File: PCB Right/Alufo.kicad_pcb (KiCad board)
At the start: 2 copper layers, 282.6 x 90.9 mm, 95 parts, among them J2 USB_C_Receptacle_USB2.0_16P_2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, J4 USB_C_Receptacle_USB2.0_16P_2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, K11 PG1350, K12 PG1350, K13 PG1350, K14 PG1350, K15 PG1350, K16 PG1350, K21 PG1350, K22 PG1350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

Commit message: Add additional pads to USB ports for strength
Also apply tweaks from left PCB to right.
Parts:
- D2: footprint Diode_SMD:D_SOD-323 -> BGK_Kicad:D_SOD-323
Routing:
- net Net-(FB2-Pad1): track 3.01 -> 2.23 mm
- net VCC: track 52.0 -> 51.2 mm
- net USB_P-: track 5.48 -> 6.10 mm
- net Row1: track 116.3 -> 115.8 mm
- net +3V3: track 85.7 -> 85.2 mm

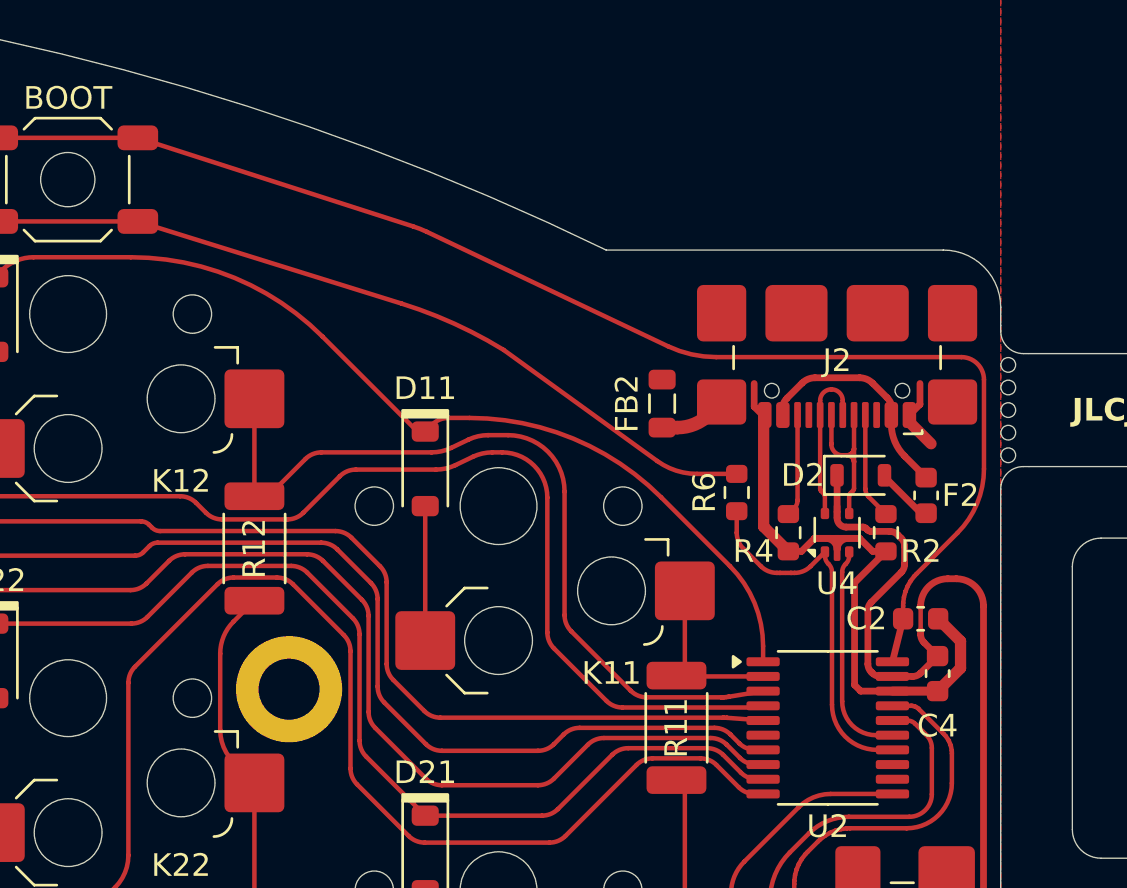
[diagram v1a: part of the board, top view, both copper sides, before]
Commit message: Move righthand USB port in
Moved port and associated components 19.05÷12mm left to account for SMD legs.
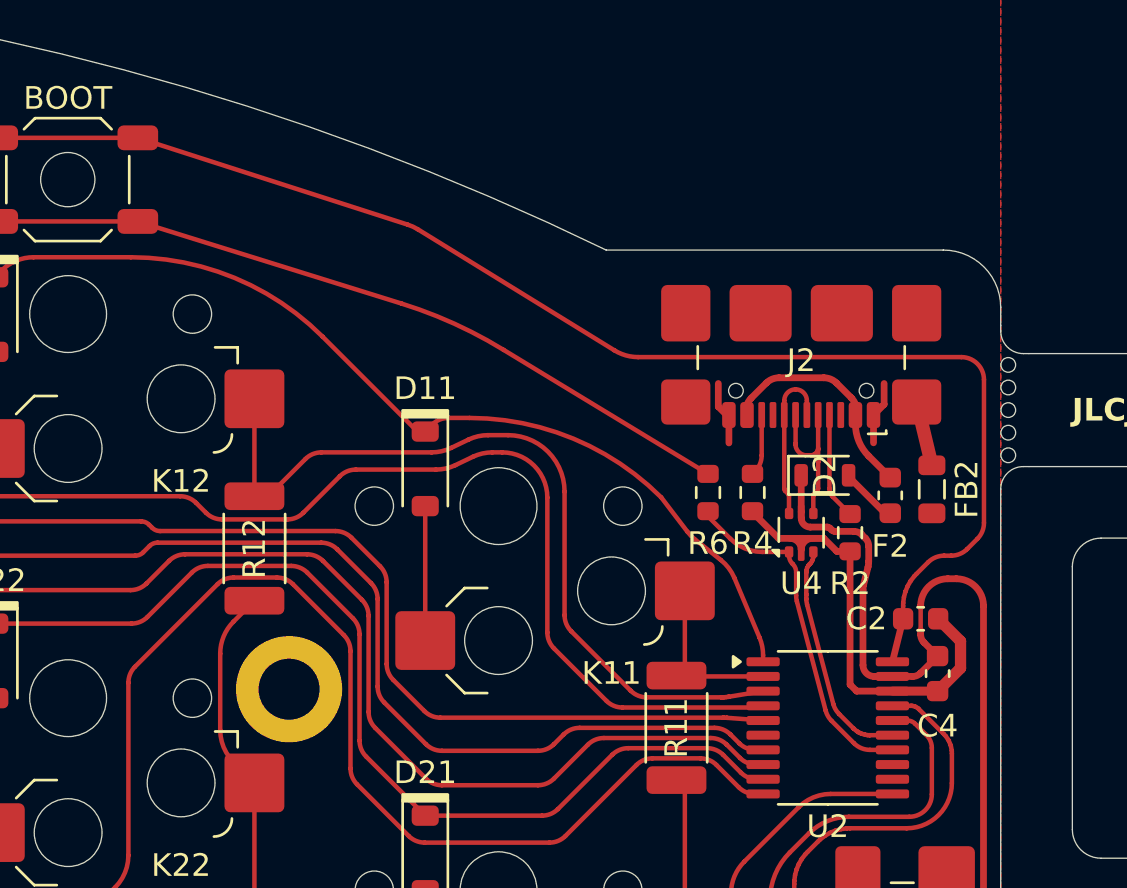
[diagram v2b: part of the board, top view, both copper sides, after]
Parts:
- removed NT2: NetTie_2, Project_Library:NetTie-2_SMD_Pad0.2mm
- moved FB2 12.5 mm to (162.1, 51.7), turned to -90 degrees
- moved R4 2.38 mm to (154.1, 51.8)
- moved D2 1.59 mm to (157.3, 51.1)
- moved F2 1.59 mm to (160.2, 51.9)
- moved J2 1.59 mm to (156.3, 44.7)
- moved R2 1.59 mm to (158.4, 53.6)
- moved U4 1.59 mm to (156.3, 53.6)
- moved R6 1.27 mm to (152.1, 51.8)
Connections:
- J2 pad S1: Net-(FB2-Pad1) -> unconnected-(J2-SHIELD-PadS1)
- J2 pad S2: unconnected-(J2-SHIELD-PadS2) -> Net-(FB2-Pad1)
- R6 pad 1: Net-(NT2-Pad2) -> USB+
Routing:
- net GND: track 33.9 -> 28.3 mm
- net Net-(NT2-Pad2): track 3.74 -> 0.00 mm
- net USB+: track 12.4 -> 15.4 mm
- net BOOT: track 35.4 -> 34.0 mm
- net Net-(J2-CC2): track 3.80 -> 2.73 mm
- net +3V3: track 85.2 -> 86.3 mm
- net Net-(FB2-Pad1): track 2.23 -> 2.88 mm

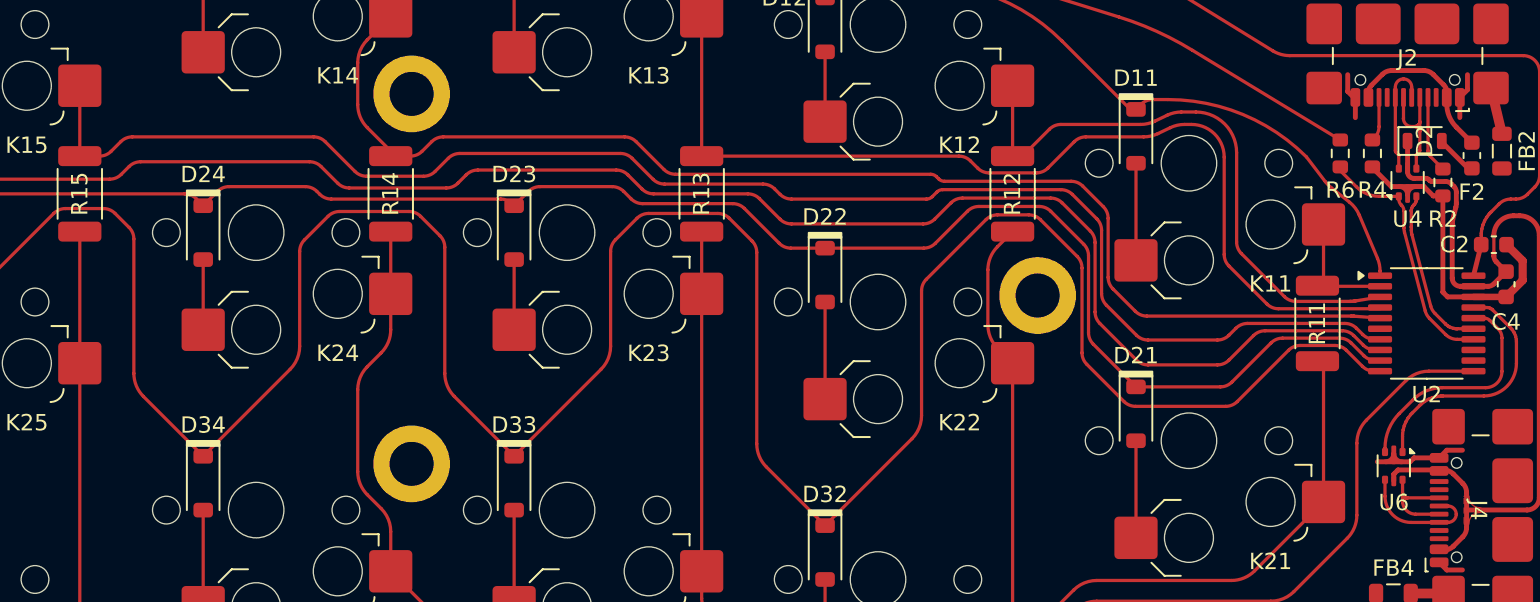
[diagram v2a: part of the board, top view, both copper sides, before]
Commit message: Remove righthand R11
Col1 now routed under MCU between K11 and K21 instead of through jumper.
Row1 and Col1 pins on MCU swapped.
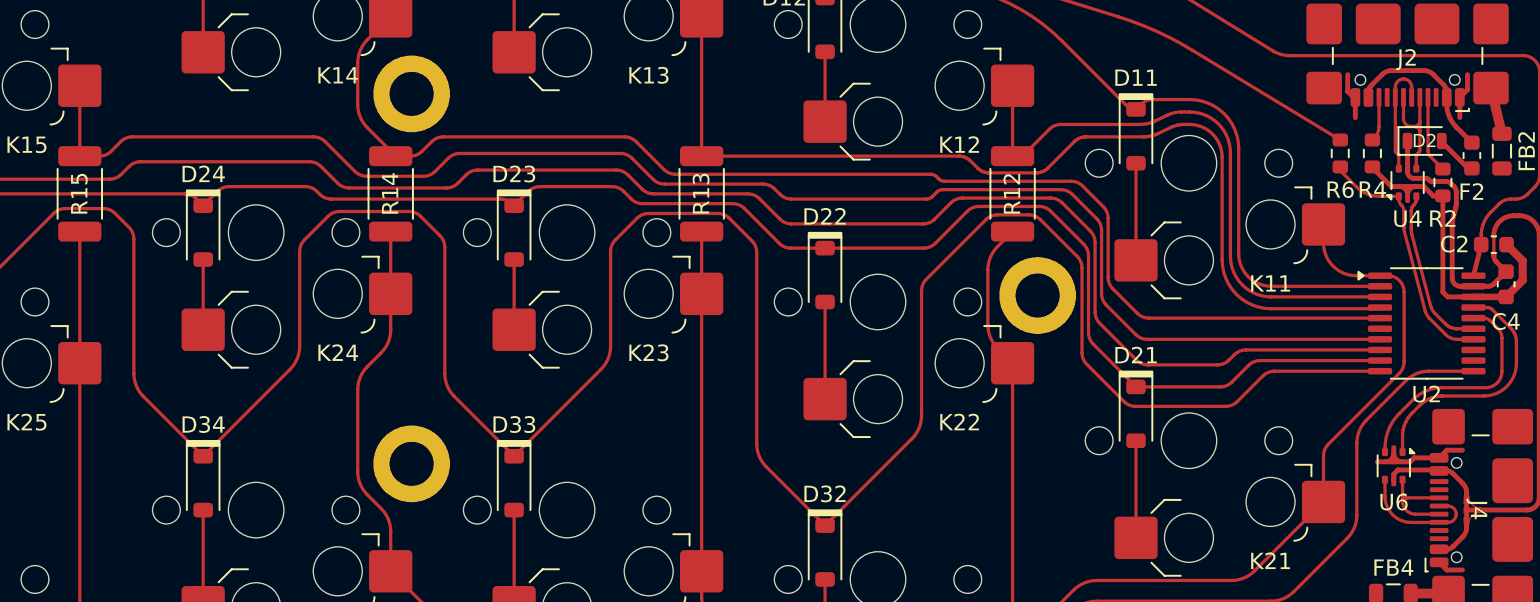
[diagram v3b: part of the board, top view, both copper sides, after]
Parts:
- removed R11: 0R, Resistor_SMD:R_2010_5025Metric
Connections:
- K21 pad 1: Col1T -> Col1
- K41 pad 1: Col1T -> Col1
- U2 pad 1: Row1 -> Col1
- U2 pad 2: Col1 -> Row1
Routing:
- net Col1: track 7.93 -> 93.6 mm
- net Col1T: track 81.4 -> 0.00 mm
- net Row1: track 115.7 -> 119.6 mm
- net Row3: track 185.6 -> 184.7 mm
- net Row2: track 122.5 -> 121.7 mm
- net Col6: track 230.6 -> 230.0 mm
- net Col2: track 35.2 -> 35.7 mm
